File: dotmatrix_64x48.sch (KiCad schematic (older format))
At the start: 73 parts, among them J7 Conn_01x04_Female, P1 CONN_01X06, P3 CONN_01X08, P4 CONN_01X08, Q2 Q_NPN_BEC, Q4 Q_NPN_BEC, SW1 SW_PUSH_SMALL_H, SW2 SW_PUSH_SMALL_H, U1 74VHC541, U16 ESP32-WROOM, U21 CM1293A-04SO, U22 CM1293A-04SO

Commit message: Almost all components has placed.
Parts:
- removed P3, P4: CONN_01X08, Pin_Headers:Pin_Header_Straight_1x08_Pitch2.54mm, symbol Connector:Conn_01x08
- removed W1, W2, W3, W4, W7: TEST_1P, Measurement_Points:Measurement_Point_Round-SMD-Pad_Small, symbol Connector:Test_Point
- added J1, J2: Conn_02x04_Odd_Even, Pin_Headers:Pin_Header_Angled_2x04_Pitch2.54mm, symbol Connector:Conn_02x04_Odd_Even
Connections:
- net labels added: LEDLOGICVDD
- wire segments 235 -> 240

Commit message: Too less PCB space.
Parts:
- removed J1, J2: Conn_02x04_Odd_Even, Pin_Headers:Pin_Header_Angled_2x04_Pitch2.54mm, symbol Connector:Conn_02x04_Odd_Even
- removed R46: 120R, Resistors_SMD:R_0603_HandSoldering, symbol device:R
- added C87: 1u, Capacitors_SMD:C_0603_HandSoldering, symbol device:C
- added D8: Led_Small, components:LED1608_Handsoldering, symbol device:LED_Small
- added J1: Conn_01x03_Female, Pin_Headers:Pin_Header_Angled_1x03_Pitch2.54mm, symbol Connector:Conn_01x03_Female
- added J2: Conn_01x03_Male, Pin_Headers:Pin_Header_Angled_1x03_Pitch2.54mm, symbol Connector:Conn_01x03_Male
- added J3: Micro_SD_Card, components:microSD_Push_Push_SMD, symbol Connector:Micro_SD_Card
- added L5: BLM21PG331SN 300R@100MHz, Capacitors_SMD:C_0805_HandSoldering, symbol device:Ferrite_Bead_Small
- added R100: 10k, Resistors_SMD:R_0603_HandSoldering, symbol device:R
- added R137: 120R, Resistors_SMD:R_0603_HandSoldering, symbol device:R
- added R138: 4.7k, Resistors_SMD:R_0603_HandSoldering, symbol device:R
- added R46: 0, components:SolderJumper_S, symbol Connector:GS2
- added U18, U27: CM1293A-04SO, TO_SOT_Packages_SMD:SOT-23-6_Handsoldering, symbol ESD_Protection:SRV05-4
- P1: footprint Pin_Headers:Pin_Header_Straight_1x08_Pitch2.54mm -> Pin_Headers:Pin_Header_Straight_1x06_Pitch2.54mm
- R125, R127: value 10k -> 120R
- R130: value 120R -> 10k
- R133, R134, R135, R136, R77, R78, R80, R81: footprint components:SolderJumper -> components:SolderJumper_S
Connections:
- net labels added: E_HS2_CLK, E_HS2_CMD, E_HS2_DATA0, E_RX2, E_TX2, HC541VDD, I2S_SPK_MCLK, IRLED_A, SD_VDD
- net labels removed: I2S_SPK_GAIN0, I2S_SPK_GAIN1, VSPI_MISO, VSPI_SCK, VSPI_SS
- wire segments 240 -> 253
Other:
- note added: "Input-only"

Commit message: Added stereo power amplifier
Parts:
- SW1, SW2: footprint Buttons_Switches_SMD:SW_SPST_FSMSM -> components:TACT_SW_SMD_Panasonic-EVPAWBD2A
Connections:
- net labels removed: IRLED_A
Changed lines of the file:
@@
 $Descr A4 11693 8268
 encoding utf-8
-Sheet 1 10
+Sheet 1 11
 Title ""
 Date ""
@@
 $EndDescr
 $Sheet
-S 700  5750 1100 150
+S 600  5450 1100 150
 U 57BB11DB
 F0 "IR_Sensor" 60
@@
 $EndSheet
 $Sheet
-S 700  6100 1100 150
+S 600  5800 1100 150
 U 5814137C
 F0 "led_matrix" 60
@@
 $EndSheet
 $Sheet
-S 700  6800 1100 150
+S 600  6500 1100 150
 U 5814137E
 F0 "column_driver" 60
@@
 $EndSheet
 $Sheet
-S 700  6450 1100 150
+S 600  6150 1100 150
 U 58141380
 F0 "row_driver" 60
@@
 $EndSheet
 $Sheet
-S 700  7150 1100 150
+S 600  6850 1100 150
 U 59A82F84
 F0 "power" 60
@@
 Connection ~ 3050 2550
 $Sheet
-S 700  7500 1100 150
+S 600  7200 1100 150
 U 5BB33F0A
 F0 "USB_UART" 60
@@
 F 0 "SW2" H 10900 1134 50  0000 C CNN
 F 1 "SW_PUSH_SMALL_H" H 10900 1134 50  0001 C CNN
-F 2 "Buttons_Switches_SMD:SW_SPST_FSMSM" H 10900 1200 50  0001 C CNN
+F 2 "components:TACT_SW_SMD_Panasonic-EVPAWBD2A" H 10900 1200 50  0001 C CNN
 F 3 "" H 10900 1200 50  0000 C CNN
 	1    10900 1000
@@
 F 0 "SW1" H 9550 984 50  0000 C CNN
 F 1 "SW_PUSH_SMALL_H" H 9550 984 50  0001 C CNN
-F 2 "Buttons_Switches_SMD:SW_SPST_FSMSM" H 9550 1050 50  0001 C CNN
+F 2 "components:TACT_SW_SMD_Panasonic-EVPAWBD2A" H 9550 1050 50  0001 C CNN
 F 3 "" H 9550 1050 50  0000 C CNN
 	1    9550 850
@@
 Wire Wire Line
 	2350 5800 2500 5800
-Text GLabel 8450 2500 0    50   Input ~ 0
-IRLED_A
 Text Label 8250 3550 0    50   ~ 0
 HC541VDD
@@
 Text GLabel 5950 5200 2    50   Input ~ 0
 E_HS2_DATA0
+$Sheet
+S 600  7550 1100 150
+U 5BE422F0
+F0 "PowerAmplifier" 50
+F1 "power_amp.sch" 50
+$EndSheet
 $EndSCHEMATC

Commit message: Switched to new kicad libraries
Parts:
- added R12, R146, R147, R42: 10R, Resistor_SMD:R_0603_1608Metric_Pad1.05x0.95mm_HandSolder, symbol dotmatrix_64x48-rescue:R-device
- C21, C22, C23, C77, C87: symbol device:C -> dotmatrix_64x48-rescue:C-device
- D8: symbol device:LED_Small -> dotmatrix_64x48-rescue:LED_Small-device
- J1: symbol Connector:Conn_01x03_Female -> dotmatrix_64x48-rescue:Conn_01x03_Female-Connector
- J2: symbol Connector:Conn_01x03_Male -> dotmatrix_64x48-rescue:Conn_01x03_Male-Connector
- J3: symbol Connector:Micro_SD_Card -> dotmatrix_64x48-rescue:Micro_SD_Card-Connector
- J7: symbol Connector:Conn_01x04_Female -> dotmatrix_64x48-rescue:Conn_01x04_Female-Connector
- L3, L5: symbol device:Ferrite_Bead_Small -> dotmatrix_64x48-rescue:Ferrite_Bead_Small-device
- P1: symbol Connector:Conn_01x06 -> dotmatrix_64x48-rescue:Conn_01x06-Connector
- Q2, Q4: symbol device:Q_NPN_BEC -> dotmatrix_64x48-rescue:Q_NPN_BEC-device
- R10, R100, R11, R118, R119, R120, R121, R122, R125, R126, R127, R128, R13, R130, R131, R132, R137, R138, R14, R15, R2, R27, R3, R34, R4, R41, R48, R49, R5, R51, R52, R53, R54, R55, R56, R57, R6, R7, R74, R75, R76, R79, R8, R9, R98: symbol device:R -> dotmatrix_64x48-rescue:R-device
- R133, R134, R135, R136, R77, R78, R80, R81: footprint components:SolderJumper_S -> components:J_0.16mm; symbol device:R -> dotmatrix_64x48-rescue:R-device
- R46: symbol Connector:GS2 -> dotmatrix_64x48-rescue:GS2-Connector
- SW1, SW2: symbol Switch:SW_Push -> dotmatrix_64x48-rescue:SW_Push-Switch
- U1: symbol Logic_74xx:74LS541 -> dotmatrix_64x48-rescue:74LS541-Logic_74xx
- U18, U21, U22, U27: symbol ESD_Protection:SRV05-4 -> dotmatrix_64x48-rescue:SRV05-4-ESD_Protection
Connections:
- net labels added: D_I2S_SPK_BCLK, D_I2S_SPK_DATA, D_I2S_SPK_LRCLK, D_I2S_SPK_MCLK
- wire segments 253 -> 258

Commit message: Prior to merge production-1.0's led matrix pattern
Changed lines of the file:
@@
-EESchema Schematic File Version 4
-LIBS:dotmatrix_64x48-cache
-EELAYER 29 0
+EESchema Schematic File Version 5
+EELAYER 30 0
 EELAYER END
 $Descr A4 11693 8268
 encoding utf-8
-Sheet 1 11
+Sheet 1 10
 Title ""
 Date ""
@@
 Comment3 ""
 Comment4 ""
+Comment5 ""
+Comment6 ""
+Comment7 ""
+Comment8 ""
+Comment9 ""
 $EndDescr
 $Sheet
@@
 Text GLabel 5950 5200 2    50   Input ~ 0
 E_HS2_DATA0
-$Sheet
-S 600  7550 1100 150
-U 5BE422F0
-F0 "PowerAmplifier" 50
-F1 "power_amp.sch" 50
-$EndSheet
 Wire Wire Line
 	5050 2400 5050 2500
@@
 Wire Wire Line
 	9150 4750 9550 4750
+Connection ~ 3050 2550
+Connection ~ 8950 3100
 $EndSCHEMATC

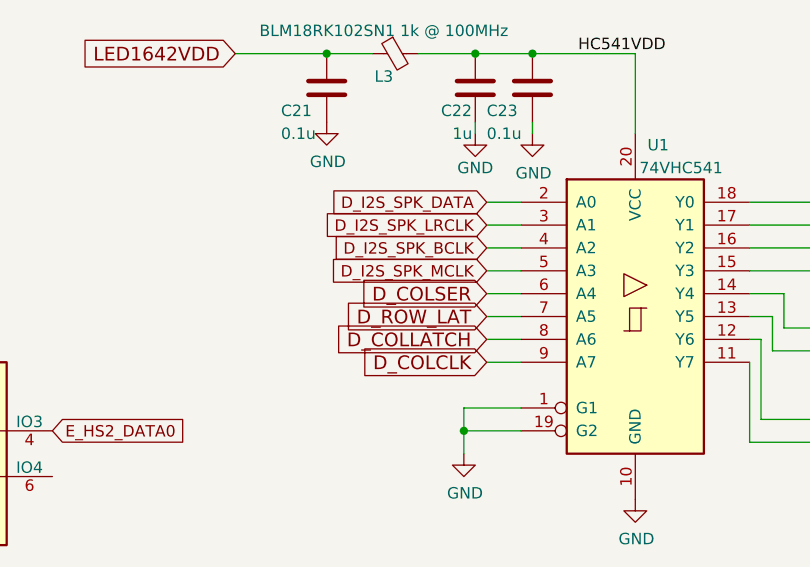
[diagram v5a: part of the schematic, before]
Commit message: Merged production-1.0's LED matrix onto current design.
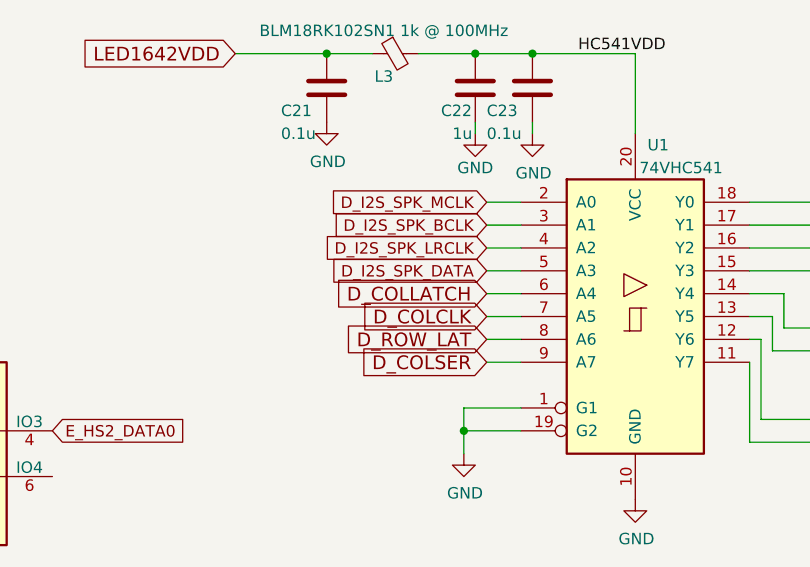
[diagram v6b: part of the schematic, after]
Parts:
- R79, R98: footprint Resistors_SMD:R_0603_HandSoldering -> Resistor_SMD:R_0603_1608Metric_Pad1.05x0.95mm_HandSolder
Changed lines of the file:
@@
 	1    0    0    -1
 $EndComp
-Text GLabel 7850 4800 0    60   Input ~ 0
+Text GLabel 7850 4600 0    60   Input ~ 0
 D_COLLATCH
+Text GLabel 7850 4700 0    60   Input ~ 0
+D_COLCLK
 Text GLabel 7850 4900 0    60   Input ~ 0
-D_COLCLK
-Text GLabel 7850 4600 0    60   Input ~ 0
 D_COLSER
 Text GLabel 10150 5250 2    60   Input ~ 0
@@
 	8500 3900 8500 3550
 Wire Wire Line
-	7850 4700 8000 4700
-Text GLabel 7850 4700 0    60   Input ~ 0
+	7850 4800 8000 4800
+Text GLabel 7850 4800 0    60   Input ~ 0
 D_ROW_LAT
 Wire Wire Line
@@
 F 0 "R98" V 10550 6050 50  0000 L CNN
 F 1 "1k" V 10650 6000 50  0000 L CNN
-F 2 "Resistors_SMD:R_0603_HandSoldering" V 10480 6150 50  0001 C CNN
+F 2 "Resistor_SMD:R_0603_1608Metric_Pad1.05x0.95mm_HandSolder" V 10480 6150 50  0001 C CNN
 F 3 "" H 10550 6150 50  0000 C CNN
 	1    10550 6150
@@
 F 0 "R79" V 8150 6050 50  0000 L CNN
 F 1 "1k" V 8250 6000 50  0000 L CNN
-F 2 "Resistors_SMD:R_0603_HandSoldering" V 8080 6150 50  0001 C CNN
+F 2 "Resistor_SMD:R_0603_1608Metric_Pad1.05x0.95mm_HandSolder" V 8080 6150 50  0001 C CNN
 F 3 "" H 8150 6150 50  0000 C CNN
 	1    8150 6150
@@
 	4350 6150 4450 6150
 Wire Wire Line
-	7850 4600 8000 4600
-Wire Wire Line
-	7850 4800 8000 4800
-Wire Wire Line
-	8000 4900 7850 4900
+	7850 4900 8000 4900
+Wire Wire Line
+	7850 4700 8000 4700
+Wire Wire Line
+	8000 4600 7850 4600
 Wire Wire Line
 	9550 4850 9500 4850
@@
 Wire Wire Line
 	9500 4650 9550 4650
+Text GLabel 7850 4300 0    50   Input ~ 0
+D_I2S_SPK_BCLK
+Text GLabel 7850 4200 0    50   Input ~ 0
+D_I2S_SPK_MCLK
 Text GLabel 7850 4400 0    50   Input ~ 0
-D_I2S_SPK_BCLK
+D_I2S_SPK_LRCLK
 Text GLabel 7850 4500 0    50   Input ~ 0
-D_I2S_SPK_MCLK
-Text GLabel 7850 4300 0    50   Input ~ 0
-D_I2S_SPK_LRCLK
-Text GLabel 7850 4200 0    50   Input ~ 0
 D_I2S_SPK_DATA
 Wire Wire Line
+	7850 4500 8000 4500
+Wire Wire Line
+	7850 4400 8000 4400
+Wire Wire Line
+	7850 4300 8000 4300
+Wire Wire Line
 	7850 4200 8000 4200
-Wire Wire Line
-	7850 4300 8000 4300
-Wire Wire Line
-	7850 4400 8000 4400
-Wire Wire Line
-	7850 4500 8000 4500
 Connection ~ 9500 4850
 Text GLabel 10000 4300 2    50   Input ~ 0
@@
 	9050 5150 9550 5150
 Wire Wire Line
-	9100 4850 9100 4700
-Wire Wire Line
-	9100 4700 9000 4700
-Wire Wire Line
 	9100 4850 9500 4850
-Wire Wire Line
-	9000 4600 9150 4600
-Wire Wire Line
-	9150 4600 9150 4750
 Wire Wire Line
 	9150 4750 9550 4750
 Connection ~ 3050 2550
 Connection ~ 8950 3100
+Wire Wire Line
+	9150 4600 9150 4750
+Wire Wire Line
+	9000 4600 9150 4600
+Wire Wire Line
+	9100 4700 9000 4700
+Wire Wire Line
+	9100 4850 9100 4700
 $EndSCHEMATC

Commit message: Before removing old style stitching vias
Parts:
- removed R128: 120R, Resistors_SMD:R_0603_HandSoldering, symbol dotmatrix_64x48-rescue:R-device
- removed R133, R134, R135, R136, R77, R78, R80, R81: 0, components:J_0.16mm, symbol dotmatrix_64x48-rescue:R-device
- removed R79, R98: 1k, Resistor_SMD:R_0603_1608Metric_Pad1.05x0.95mm_HandSolder, symbol dotmatrix_64x48-rescue:R-device
- removed U18: CM1293A-04SO, TO_SOT_Packages_SMD:SOT-23-6_Handsoldering, symbol dotmatrix_64x48-rescue:SRV05-4-ESD_Protection
- added R99: 10k, Resistor_SMD:R_0603_1608Metric_Pad1.05x0.95mm_HandSolder, symbol dotmatrix_64x48-rescue:R-device
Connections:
- net labels removed: CC_GUARD0, CC_GUARD1, RC_GUARD0, RC_GUARD1, VSPI_MOSI
- wire segments 258 -> 218
- no-connect marks 7 -> 8

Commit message: Almost done drawing pcb tracks
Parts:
- R2, R74: value 10R -> 120R
- renumbered R46 to JP1
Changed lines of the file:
@@
 AR Path="/5BB4924C" Ref="R2"  Part="1"
 F 0 "R2" V 5400 1200 50  0000 L CNN
-F 1 "10R" V 5450 1000 50  0000 L CNN
+F 1 "120R" V 5450 1000 50  0000 L CNN
 F 2 "Resistors_SMD:R_0603_HandSoldering" V 5330 1300 50  0001 C CNN
 F 3 "" H 5400 1300 50  0000 C CNN
@@
 AR Path="/5BD92997" Ref="R74"  Part="1"
 F 0 "R74" V 5400 1400 50  0000 L CNN
-F 1 "10R" V 5450 1200 50  0000 L CNN
+F 1 "120R" V 5450 1200 50  0000 L CNN
 F 2 "Resistors_SMD:R_0603_HandSoldering" V 5330 1500 50  0001 C CNN
 F 3 "" H 5400 1500 50  0000 C CNN
@@
 P 2700 5800
 AR Path="/59A8E319/5C0A619A" Ref="R?"  Part="1"
-AR Path="/5C0A619A" Ref="R46"  Part="1"
-F 0 "R46" V 2700 5700 50  0000 L CNN
+AR Path="/5C0A619A" Ref="JP1"  Part="1"
+F 0 "JP1" V 2800 5700 50  0000 L CNN
 F 1 "0" V 2600 5900 50  0001 L CNN
 F 2 "components:SolderJumper_S" V 2630 5800 50  0001 C CNN
